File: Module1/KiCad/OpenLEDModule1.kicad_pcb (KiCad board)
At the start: 2 copper layers, 29.2 x 29.2 mm, 8 parts, among them P1 CONN_01X02, P2 CONN_01X02

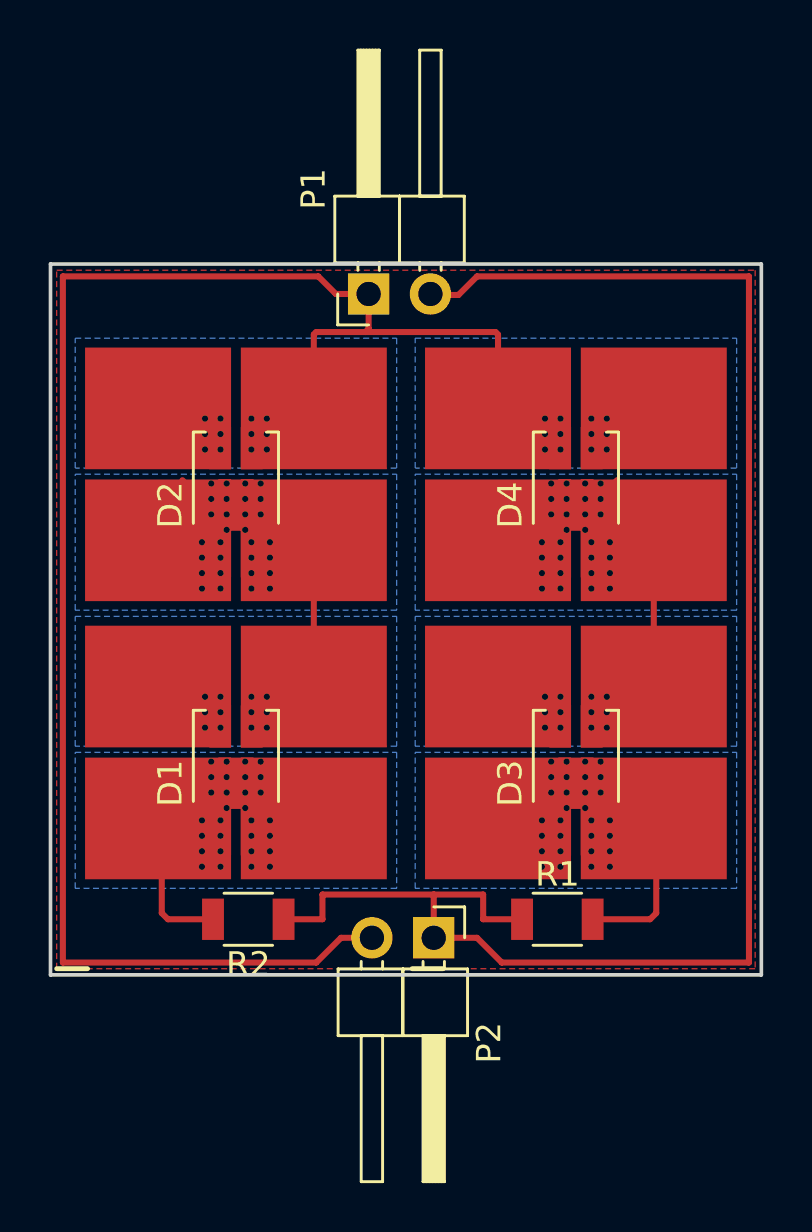
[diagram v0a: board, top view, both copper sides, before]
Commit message: Several fixes to resolve review comments (thermal via connections, cooling pads, footprint, past and mask layers, resistors, holes, tracks)
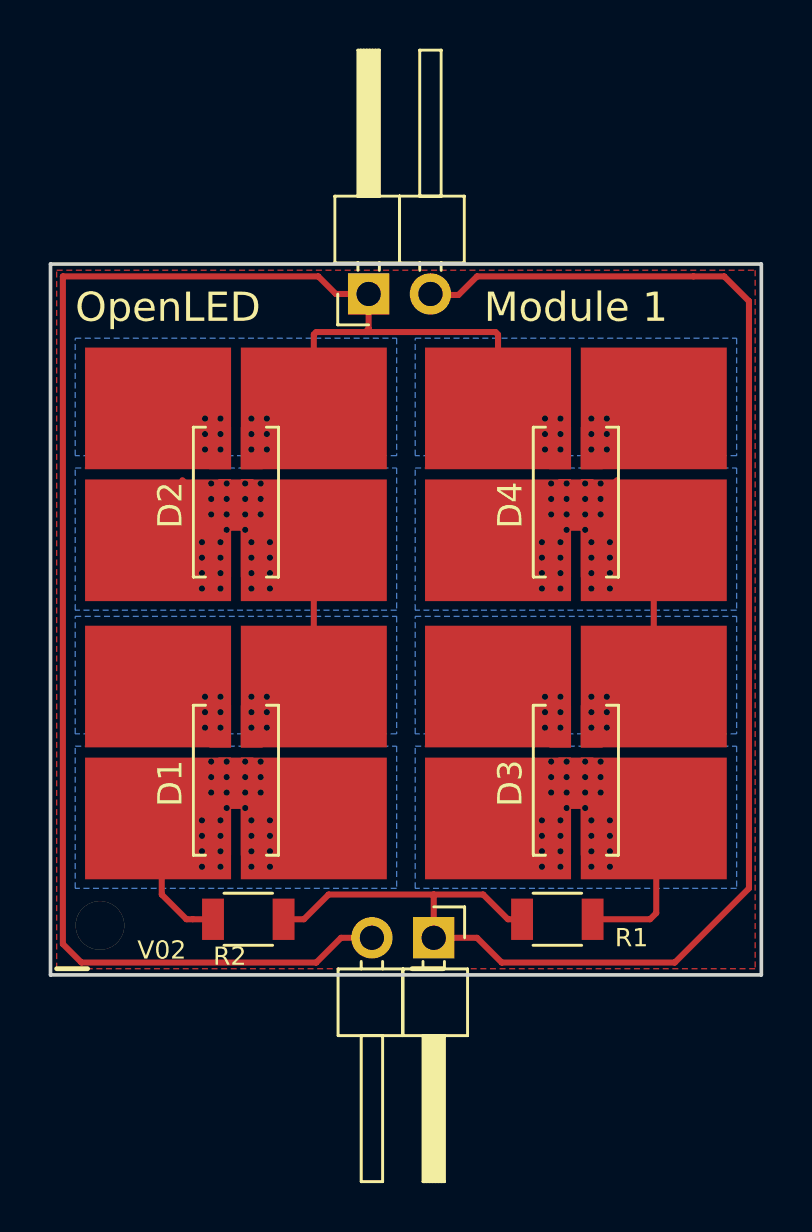
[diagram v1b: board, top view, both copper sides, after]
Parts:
- added ?: , OpenLed:DRILLHOLE, F.Cu at (138.9, 97.3)
- added ?: , OpenLed:DRILLHOLE, F.Cu at (164.8, 97.5)
- P1: value CONN_01X02 -> CONN2
- P2: value CONN_01X02 -> CONN1
- R1, R2: value R -> 15
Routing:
- net GND: track 69.6 -> 81.2 mm
- net Net-(D3-Pad1): track 7.44 -> 13.9 mm
- net +24V: track 68.6 -> 65.0 mm
- added copper zone on B.Cu, net GND
- added copper zone on B.Cu, net Net-(D1-Pad1)
- added copper zone on B.Cu, net Net-(D1-Pad2)
- added copper zone on B.Cu, net Net-(D3-Pad1)
- added copper zone on B.Cu, net Net-(D3-Pad2)
- removed copper zone on B.Cu, net (none)
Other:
- board text added: "V02"
- board text removed: "V001"
